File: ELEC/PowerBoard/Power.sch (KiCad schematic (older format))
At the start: 2 parts, among them J1 CONN_01X08, J2 CONN_01X08

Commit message: Added roadmap, worked on power board
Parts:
- added C1, C2, C3, C4: 220uF, Capacitors_SMD:CP_Elec_8x10.5, symbol CP
- added C5, C6, C7: 10uF, Capacitors_SMD:C_1206, symbol C
- added C8: 0.1uF, Capacitors_SMD:C_0805, symbol C
- added J3: Barrel_Jack, Connectors_Barrel.pretty:PJ-082BH, symbol Barrel_Jack
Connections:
- net +24V: now also C1.1, C2.1, C3.1, C4.1, C5.1, C6.1, C7.1, C8.1, J3.1
- net GND: now also C1.2, C2.2, C3.2, C4.2, C5.2, C6.2, C7.2, C8.2, J3.2, J3.3
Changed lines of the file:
@@
 LIBS:device
 LIBS:power
+LIBS:Power-cache
 EELAYER 25 0
 EELAYER END
@@
 NoConn ~ 2650 3650
 NoConn ~ 2650 3750
+$Comp
+L Barrel_Jack J3
+U 1 1 59628A55
+P 4500 3350
+F 0 "J3" H 4500 3560 50  0000 C CNN
+F 1 "Barrel_Jack" H 4500 3175 50  0000 C CNN
+F 2 "Connectors_Barrel.pretty:PJ-082BH" H 4550 3310 50  0001 C CNN
+F 3 "" H 4550 3310 50  0001 C CNN
+	1    4500 3350
+	1    0    0    -1
+$EndComp
+$Comp
+L +24V #PWR04
+U 1 1 59628BF8
+P 5200 3100
+F 0 "#PWR04" H 5200 2950 50  0001 C CNN
+F 1 "+24V" H 5200 3240 50  0000 C CNN
+F 2 "" H 5200 3100 50  0001 C CNN
+F 3 "" H 5200 3100 50  0001 C CNN
+	1    5200 3100
+	1    0    0    -1
+$EndComp
+Wire Wire Line
+	5200 3250 5200 3100
+Wire Wire Line
+	4800 3350 4800 3600
+Wire Wire Line
+	4800 3600 5200 3600
+Wire Wire Line
+	5200 3550 5200 3700
+Connection ~ 4800 3450
+$Comp
+L GND #PWR05
+U 1 1 59628CB8
+P 5200 3700
+F 0 "#PWR05" H 5200 3450 50  0001 C CNN
+F 1 "GND" H 5200 3550 50  0000 C CNN
+F 2 "" H 5200 3700 50  0001 C CNN
+F 3 "" H 5200 3700 50  0001 C CNN
+	1    5200 3700
+	1    0    0    -1
+$EndComp
+$Comp
+L CP C1
+U 1 1 59628D75
+P 5400 3400
+F 0 "C1" H 5425 3500 50  0000 L CNN
+F 1 "220uF" H 5425 3300 50  0000 L CNN
+F 2 "Capacitors_SMD:CP_Elec_8x10.5" H 5438 3250 50  0001 C CNN
+F 3 "" H 5400 3400 50  0001 C CNN
+F 4 "EEE-1VA221UP" H 5400 3400 60  0001 C CNN "Part Number"
+	1    5400 3400
+	1    0    0    -1
+$EndComp
+Connection ~ 5200 3250
+Connection ~ 5200 3600
+$Comp
+L C C6
+U 1 1 59628F1D
+P 6800 3400
+F 0 "C6" H 6825 3500 50  0000 L CNN
+F 1 "10uF" H 6825 3300 50  0000 L CNN
+F 2 "Capacitors_SMD:C_1206" H 6838 3250 50  0001 C CNN
+F 3 "" H 6800 3400 50  0001 C CNN
+	1    6800 3400
+	1    0    0    -1
+$EndComp
+$Comp
+L CP C2
+U 1 1 59629990
+P 5750 3400
+F 0 "C2" H 5775 3500 50  0000 L CNN
+F 1 "220uF" H 5775 3300 50  0000 L CNN
+F 2 "Capacitors_SMD:CP_Elec_8x10.5" H 5788 3250 50  0001 C CNN
+F 3 "" H 5750 3400 50  0001 C CNN
+F 4 "EEE-1VA221UP" H 5750 3400 60  0001 C CNN "Part Number"
+	1    5750 3400
+	1    0    0    -1
+$EndComp
+$Comp
+L CP C3
+U 1 1 596299C2
+P 6100 3400
+F 0 "C3" H 6125 3500 50  0000 L CNN
+F 1 "220uF" H 6125 3300 50  0000 L CNN
+F 2 "Capacitors_SMD:CP_Elec_8x10.5" H 6138 3250 50  0001 C CNN
+F 3 "" H 6100 3400 50  0001 C CNN
+F 4 "EEE-1VA221UP" H 6100 3400 60  0001 C CNN "Part Number"
+	1    6100 3400
+	1    0    0    -1
+$EndComp
+$Comp
+L CP C4
+U 1 1 596299F7
+P 6450 3400
+F 0 "C4" H 6475 3500 50  0000 L CNN
+F 1 "220uF" H 6475 3300 50  0000 L CNN
+F 2 "Capacitors_SMD:CP_Elec_8x10.5" H 6488 3250 50  0001 C CNN
+F 3 "" H 6450 3400 50  0001 C CNN
+F 4 "EEE-1VA221UP" H 6450 3400 60  0001 C CNN "Part Number"
+	1    6450 3400
+	1    0    0    -1
+$EndComp
+$Comp
+L C C5
+U 1 1 59629A98
+P 7100 3400
+F 0 "C5" H 7125 3500 50  0000 L CNN
+F 1 "10uF" H 7125 3300 50  0000 L CNN
+F 2 "Capacitors_SMD:C_1206" H 7138 3250 50  0001 C CNN
+F 3 "" H 7100 3400 50  0001 C CNN
+	1    7100 3400
+	1    0    0    -1
+$EndComp
+$Comp
+L C C7
+U 1 1 59629ADF
+P 7400 3400
+F 0 "C7" H 7425 3500 50  0000 L CNN
+F 1 "10uF" H 7425 3300 50  0000 L CNN
+F 2 "Capacitors_SMD:C_1206" H 7438 3250 50  0001 C CNN
+F 3 "" H 7400 3400 50  0001 C CNN
+	1    7400 3400
+	1    0    0    -1
+$EndComp
+$Comp
+L C C8
+U 1 1 59629B15
+P 7700 3400
+F 0 "C8" H 7725 3500 50  0000 L CNN
+F 1 "0.1uF" H 7725 3300 50  0000 L CNN
+F 2 "Capacitors_SMD:C_0805" H 7738 3250 50  0001 C CNN
+F 3 "" H 7700 3400 50  0001 C CNN
+	1    7700 3400
+	1    0    0    -1
+$EndComp
+Wire Wire Line
+	4800 3250 7700 3250
+Connection ~ 5400 3250
+Connection ~ 5750 3250
+Connection ~ 6100 3250
+Connection ~ 6450 3250
+Connection ~ 6800 3250
+Connection ~ 7100 3250
+Connection ~ 7400 3250
+Wire Wire Line
+	5200 3550 7700 3550
+Connection ~ 5400 3550
+Connection ~ 5750 3550
+Connection ~ 6100 3550
+Connection ~ 6450 3550
+Connection ~ 6800 3550
+Connection ~ 7100 3550
+Connection ~ 7400 3550
 $EndSCHEMATC

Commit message: Worked on power distrobution PCB
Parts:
- removed C5, C6, C7: 10uF, Capacitors_SMD:C_1206, symbol C
- removed C8: 0.1uF, Capacitors_SMD:C_0805, symbol C
- added J4: XT60 Connector, Connectors_Battery:XT60_Inline, symbol CONN_01X02
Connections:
- wire segments 20 -> 23
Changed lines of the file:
@@
 	1    0    0    -1
 $EndComp
-Wire Wire Line
-	2350 3050 2650 3050
 Text Label 2650 3050 0    60   ~ 0
 SYNC
@@
 	1    0    0    -1
 $EndComp
-Wire Wire Line
-	10250 3100 10250 3400
-Connection ~ 10250 3300
-Connection ~ 10250 3200
-Connection ~ 10250 3250
-Wire Wire Line
-	10250 3250 10050 3250
-Wire Wire Line
-	10050 3250 10050 3050
-Wire Wire Line
-	10250 3500 10250 3800
-Connection ~ 10250 3600
-Connection ~ 10250 3700
 $Comp
 L GND #PWR03
@@
 	1    0    0    -1
 $EndComp
-Wire Wire Line
-	10250 3650 10050 3650
-Wire Wire Line
-	10050 3650 10050 3850
-Connection ~ 10250 3650
 Text Label 2650 3250 0    60   ~ 0
 AUX_R
 Text Label 2650 3350 0    60   ~ 0
 AUX_L
-Wire Wire Line
-	2650 3250 2350 3250
-Wire Wire Line
-	2350 3350 2650 3350
-Wire Wire Line
-	2950 3150 2350 3150
-Wire Wire Line
-	2350 3450 2650 3450
-Wire Wire Line
-	2350 3550 2650 3550
-Wire Wire Line
-	2350 3650 2650 3650
-Wire Wire Line
-	2350 3750 2650 3750
 NoConn ~ 2650 3450
 NoConn ~ 2650 3550
@@
 	1    0    0    -1
 $EndComp
-Wire Wire Line
-	5200 3250 5200 3100
-Wire Wire Line
-	4800 3350 4800 3600
-Wire Wire Line
-	4800 3600 5200 3600
-Wire Wire Line
-	5200 3550 5200 3700
-Connection ~ 4800 3450
 $Comp
 L GND #PWR05
@@
 	1    0    0    -1
 $EndComp
-Connection ~ 5200 3250
-Connection ~ 5200 3600
-$Comp
-L C C6
-U 1 1 59628F1D
-P 6800 3400
-F 0 "C6" H 6825 3500 50  0000 L CNN
-F 1 "10uF" H 6825 3300 50  0000 L CNN
-F 2 "Capacitors_SMD:C_1206" H 6838 3250 50  0001 C CNN
-F 3 "" H 6800 3400 50  0001 C CNN
-	1    6800 3400
-	1    0    0    -1
-$EndComp
 $Comp
 L CP C2
@@
 $EndComp
 $Comp
-L C C5
-U 1 1 59629A98
-P 7100 3400
-F 0 "C5" H 7125 3500 50  0000 L CNN
-F 1 "10uF" H 7125 3300 50  0000 L CNN
-F 2 "Capacitors_SMD:C_1206" H 7138 3250 50  0001 C CNN
-F 3 "" H 7100 3400 50  0001 C CNN
-	1    7100 3400
-	1    0    0    -1
-$EndComp
-$Comp
-L C C7
-U 1 1 59629ADF
-P 7400 3400
-F 0 "C7" H 7425 3500 50  0000 L CNN
-F 1 "10uF" H 7425 3300 50  0000 L CNN
-F 2 "Capacitors_SMD:C_1206" H 7438 3250 50  0001 C CNN
-F 3 "" H 7400 3400 50  0001 C CNN
-	1    7400 3400
-	1    0    0    -1
-$EndComp
-$Comp
-L C C8
-U 1 1 59629B15
-P 7700 3400
-F 0 "C8" H 7725 3500 50  0000 L CNN
-F 1 "0.1uF" H 7725 3300 50  0000 L CNN
-F 2 "Capacitors_SMD:C_0805" H 7738 3250 50  0001 C CNN
-F 3 "" H 7700 3400 50  0001 C CNN
-	1    7700 3400
-	1    0    0    -1
-$EndComp
-Wire Wire Line
-	4800 3250 7700 3250
+L CONN_01X02 J4
+U 1 1 597010A4
+P 4500 4150
+F 0 "J4" H 4500 4300 50  0000 C CNN
+F 1 "XT60 Connector" H 4500 4400 50  0000 C CNN
+F 2 "Connectors_Battery:XT60_Inline" H 4500 4150 50  0001 C CNN
+F 3 "" H 4500 4150 50  0001 C CNN
+	1    4500 4150
+	-1   0    0    -1
+$EndComp
+$Comp
+L GND #PWR?
+U 1 1 59701954
+P 4850 4400
+F 0 "#PWR?" H 4850 4150 50  0001 C CNN
+F 1 "GND" H 4850 4250 50  0000 C CNN
+F 2 "" H 4850 4400 50  0001 C CNN
+F 3 "" H 4850 4400 50  0001 C CNN
+	1    4850 4400
+	1    0    0    -1
+$EndComp
+Wire Wire Line
+	2350 3050 2650 3050
+Wire Wire Line
+	10250 3100 10250 3400
+Connection ~ 10250 3300
+Connection ~ 10250 3200
+Connection ~ 10250 3250
+Wire Wire Line
+	10250 3250 10050 3250
+Wire Wire Line
+	10050 3250 10050 3050
+Wire Wire Line
+	10250 3500 10250 3800
+Connection ~ 10250 3600
+Connection ~ 10250 3700
+Wire Wire Line
+	10250 3650 10050 3650
+Wire Wire Line
+	10050 3650 10050 3850
+Connection ~ 10250 3650
+Wire Wire Line
+	2650 3250 2350 3250
+Wire Wire Line
+	2350 3350 2650 3350
+Wire Wire Line
+	2950 3150 2350 3150
+Wire Wire Line
+	2350 3450 2650 3450
+Wire Wire Line
+	2350 3550 2650 3550
+Wire Wire Line
+	2350 3650 2650 3650
+Wire Wire Line
+	2350 3750 2650 3750
+Wire Wire Line
+	5200 3250 5200 3100
+Wire Wire Line
+	4800 3350 4800 3600
+Wire Wire Line
+	4800 3600 5200 3600
+Wire Wire Line
+	5200 3550 5200 3700
+Connection ~ 4800 3450
+Connection ~ 5200 3250
+Connection ~ 5200 3600
+Wire Wire Line
+	4800 3250 6450 3250
 Connection ~ 5400 3250
 Connection ~ 5750 3250
 Connection ~ 6100 3250
-Connection ~ 6450 3250
-Connection ~ 6800 3250
-Connection ~ 7100 3250
-Connection ~ 7400 3250
-Wire Wire Line
-	5200 3550 7700 3550
 Connection ~ 5400 3550
 Connection ~ 5750 3550
 Connection ~ 6100 3550
-Connection ~ 6450 3550
-Connection ~ 6800 3550
-Connection ~ 7100 3550
-Connection ~ 7400 3550
+Wire Wire Line
+	5200 3550 6450 3550
+Wire Wire Line
+	4700 4200 4850 4200
+Wire Wire Line
+	4850 4200 4850 4400
+Wire Wire Line
+	4700 4100 5850 4100
 $EndSCHEMATC

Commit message: Did a whole whack on the power PCB
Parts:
- added J5: CONN_02X03, Pin_Headers:Pin_Header_Straight_2x03_Pitch1.27mm, symbol CONN_02X03
- added Q1: MOSFET_8PIN, Housings_SOIC.pretty:SOIC-8_3.9x4.9mm_Pitch1.27mm, symbol MOSFET_8PIN
- added R1, R5, R6, R7, Ry1: 1M, Resistors_SMD:R_0805, symbol R
- added R2: 422K, Resistors_SMD:R_0805, symbol R
- added R3: 316K, Resistors_SMD:R_0805, symbol R
- added R4: 243K, Resistors_SMD:R_0805, symbol R
- added Rh1: 1.32M, Resistors_SMD:R_0805, symbol R
- added Rx1: 220K, Resistors_SMD:R_0805, symbol R
- added U1: LM9036MX, Housings_SOIC.pretty:SOIC-8_3.9x4.9mm_Pitch1.27mm, symbol LM9036MX
- added U2: LMV358, Housings_SOIC.pretty:SOIC-8_3.9x4.9mm_Pitch1.27mm, symbol LMV358
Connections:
- net labels added: +5V, Vref
- wire segments 23 -> 85
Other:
- note added: "4,5,6 cell selector"
- note added: "WARNING: Never plug in XT60 connector (Battery) at time same time as the barrel jack!!!"
- moved on the sheet: C1, C2, C3, C4, J3, J4

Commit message: Finished Power PCB
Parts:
- added C10: 1uF, Capacitors_SMD:C_0805, symbol C
- added C5, C7, C9: 100nF, Capacitors_SMD:C_0805, symbol C
- added C6, C8: 10uF, Capacitors_SMD:C_0805, symbol C
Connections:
- net +24V: now also C5.1, C6.1
- net +5V: now also C10.1, C7.1, C8.1, C9.1
- net GND: now also C10.2, C5.2, C6.2, C7.2, C8.2, C9.2
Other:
- moved on the sheet: J5, R1, R2, R3, R4

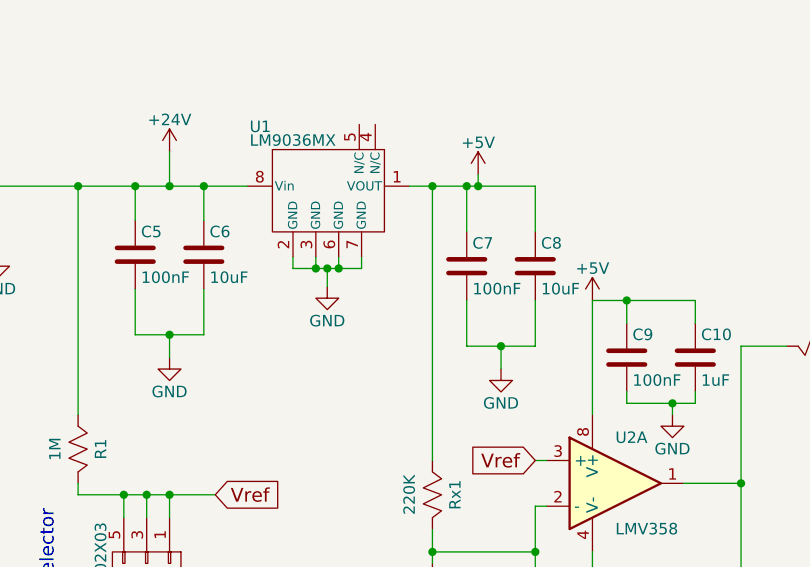
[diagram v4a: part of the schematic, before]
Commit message: -Filled in P/N -Generated BOM -Ordered PCBs
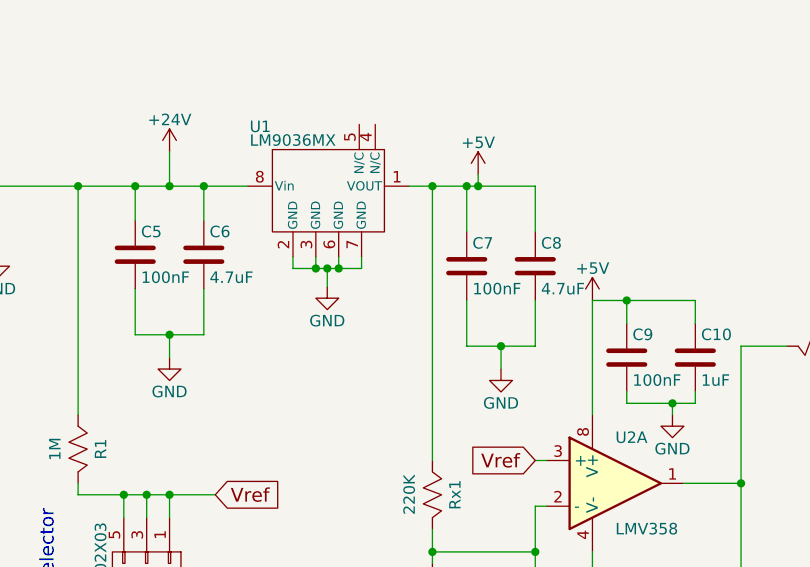
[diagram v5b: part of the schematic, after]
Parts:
- C10: Part Number (none) -> CL21B105KBFNNNE
- C5, C7, C9: Part Number (none) -> CL21B103KBANNNC
- C6, C8: value 10uF -> 4.7uF; Part Number (none) -> CL21A475KLCLQNC
- J3: Part Number (none) -> PJ-082BH
- J5: Part Number (none) -> 20021111-00006T4LF
- Q1: Part Number (none) -> AO4576
- R1, R5, R6, R7, Ry1: Part Number (none) -> ERJ-6GEYJ105V
- R2: Part Number (none) -> ERJ-6ENF4223V
- R3: Part Number (none) -> ERJ-6ENF3163V
- R4: Part Number (none) -> ERJ-6ENF2433V
- Rh1: Part Number (none) -> ERJ-6ENF1334V
- Rx1: Part Number (none) -> ERJ-6GEYJ224V
- U1: Part Number (none) -> LM9036MX-5.0/NOPB
- U2: Part Number (none) -> LMV358MX/NOPB
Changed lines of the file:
@@
 SYNC
 $Comp
-L GNDA #PWR1
+L GNDA #PWR01
 U 1 1 593E4897
 P 2950 3150
-F 0 "#PWR1" H 2950 2900 50  0001 C CNN
+F 0 "#PWR01" H 2950 2900 50  0001 C CNN
 F 1 "GNDA" V 2950 2900 50  0000 C CNN
 F 2 "" H 2950 3150 50  0001 C CNN
@@
 $EndComp
 $Comp
-L +24V #PWR19
+L +24V #PWR02
 U 1 1 593E5732
 P 10050 3050
-F 0 "#PWR19" H 10050 2900 50  0001 C CNN
+F 0 "#PWR02" H 10050 2900 50  0001 C CNN
 F 1 "+24V" H 10050 3190 50  0000 C CNN
 F 2 "" H 10050 3050 50  0001 C CNN
@@
 F 2 "Connectors_Barrel.pretty:PJ-082BH" H 4600 2410 50  0001 C CNN
 F 3 "" H 4600 2410 50  0001 C CNN
+F 4 "PJ-082BH" H 4550 2450 60  0001 C CNN "Part Number"
 	1    4550 2450
 	1    0    0    -1
 $EndComp
 $Comp
-L +24V #PWR7
+L +24V #PWR03
 U 1 1 59628BF8
 P 5250 2200
-F 0 "#PWR7" H 5250 2050 50  0001 C CNN
+F 0 "#PWR03" H 5250 2050 50  0001 C CNN
 F 1 "+24V" H 5250 2340 50  0000 C CNN
 F 2 "" H 5250 2200 50  0001 C CNN
@@
 $EndComp
 $Comp
-L GND #PWR8
+L GND #PWR04
 U 1 1 59628CB8
 P 5250 2800
-F 0 "#PWR8" H 5250 2550 50  0001 C CNN
+F 0 "#PWR04" H 5250 2550 50  0001 C CNN
 F 1 "GND" H 5250 2650 50  0000 C CNN
 F 2 "" H 5250 2800 50  0001 C CNN
@@
 $EndComp
 $Comp
-L GND #PWR2
+L GND #PWR05
 U 1 1 59701954
 P 3400 4550
-F 0 "#PWR2" H 3400 4300 50  0001 C CNN
+F 0 "#PWR05" H 3400 4300 50  0001 C CNN
 F 1 "GND" H 3400 4400 50  0000 C CNN
 F 2 "" H 3400 4550 50  0001 C CNN
@@
 $EndComp
 $Comp
-L GND #PWR6
+L GND #PWR06
 U 1 1 598A7FE8
 P 4840 4690
-F 0 "#PWR6" H 4840 4440 50  0001 C CNN
+F 0 "#PWR06" H 4840 4440 50  0001 C CNN
 F 1 "GND" H 4840 4540 50  0000 C CNN
 F 2 "" H 4840 4690 50  0001 C CNN
@@
 $EndComp
 $Comp
-L +5V #PWR10
+L +5V #PWR07
 U 1 1 598A84C1
 P 5500 4200
-F 0 "#PWR10" H 5500 4050 50  0001 C CNN
+F 0 "#PWR07" H 5500 4050 50  0001 C CNN
 F 1 "+5V" H 5500 4340 50  0000 C CNN
 F 2 "" H 5500 4200 50  0001 C CNN
@@
 F 2 "Housings_SOIC.pretty:SOIC-8_3.9x4.9mm_Pitch1.27mm" H 6100 5550 50  0001 C CNN
 F 3 "" H 6100 5550 50  0001 C CNN
+F 4 "LMV358MX/NOPB" H 6100 5550 60  0001 C CNN "Part Number"
 	1    6100 5550
 	1    0    0    -1
@@
 F 2 "Resistors_SMD:R_0805" V 3680 5400 50  0001 C CNN
 F 3 "" H 3750 5400 50  0001 C CNN
+F 4 "ERJ-6GEYJ105V" V 3750 5400 60  0001 C CNN "Part Number"
 	1    3750 5400
 	1    0    0    -1
@@
 F 2 "Resistors_SMD:R_0805" V 3680 6600 50  0001 C CNN
 F 3 "" H 3750 6600 50  0001 C CNN
+F 4 "ERJ-6ENF4223V" V 3750 6600 60  0001 C CNN "Part Number"
 	1    3750 6600
 	1    0    0    -1
 $EndComp
 $Comp
-L +5V #PWR12
+L +5V #PWR08
 U 1 1 598A865B
 P 6000 4750
-F 0 "#PWR12" H 6000 4600 50  0001 C CNN
+F 0 "#PWR08" H 6000 4600 50  0001 C CNN
 F 1 "+5V" H 6000 4890 50  0000 C CNN
 F 2 "" H 6000 4750 50  0001 C CNN
@@
 $EndComp
 $Comp
-L GND #PWR13
+L GND #PWR09
 U 1 1 598A86D5
 P 6000 6000
-F 0 "#PWR13" H 6000 5750 50  0001 C CNN
+F 0 "#PWR09" H 6000 5750 50  0001 C CNN
 F 1 "GND" H 6000 5850 50  0000 C CNN
 F 2 "" H 6000 6000 50  0001 C CNN
@@
 F 2 "Resistors_SMD:R_0805" V 3980 6600 50  0001 C CNN
 F 3 "" H 4050 6600 50  0001 C CNN
+F 4 "ERJ-6ENF3163V" V 4050 6600 60  0001 C CNN "Part Number"
 	1    4050 6600
 	1    0    0    -1
@@
 F 2 "Resistors_SMD:R_0805" V 4280 6600 50  0001 C CNN
 F 3 "" H 4350 6600 50  0001 C CNN
+F 4 "ERJ-6ENF2433V" V 4350 6600 60  0001 C CNN "Part Number"
 	1    4350 6600
 	1    0    0    -1
@@
 F 2 "Pin_Headers:Pin_Header_Straight_2x03_Pitch1.27mm" H 4050 4750 50  0001 C CNN
 F 3 "" H 4050 4750 50  0001 C CNN
+F 4 "20021111-00006T4LF" H 4050 5950 60  0001 C CNN "Part Number"
 	1    4050 5950
 	0    1    1    0
 $EndComp
 $Comp
-L GND #PWR3
+L GND #PWR010
 U 1 1 598A9A51
 P 4050 6900
-F 0 "#PWR3" H 4050 6650 50  0001 C CNN
+F 0 "#PWR010" H 4050 6650 50  0001 C CNN
 F 1 "GND" H 4050 6750 50  0000 C CNN
 F 2 "" H 4050 6900 50  0001 C CNN
@@
 F 2 "Resistors_SMD:R_0805" V 5230 5600 50  0001 C CNN
 F 3 "" H 5300 5600 50  0001 C CNN
+F 4 "ERJ-6GEYJ224V" V 5300 5600 60  0001 C CNN "Part Number"
 	1    5300 5600
 	1    0    0    -1
@@
 F 2 "Resistors_SMD:R_0805" V 5230 6050 50  0001 C CNN
 F 3 "" H 5300 6050 50  0001 C CNN
+F 4 "ERJ-6GEYJ105V" V 5300 6050 60  0001 C CNN "Part Number"
 	1    5300 6050
 	1    0    0    -1
@@
 F 2 "Resistors_SMD:R_0805" V 6130 6400 50  0001 C CNN
 F 3 "" H 6200 6400 50  0001 C CNN
+F 4 "ERJ-6ENF1334V" V 6200 6400 60  0001 C CNN "Part Number"
 	1    6200 6400
 	0    1    1    0
 $EndComp
 $Comp
-L GND #PWR9
+L GND #PWR011
 U 1 1 598AB730
 P 5300 6300
-F 0 "#PWR9" H 5300 6050 50  0001 C CNN
+F 0 "#PWR011" H 5300 6050 50  0001 C CNN
 F 1 "GND" H 5300 6150 50  0000 C CNN
 F 2 "" H 5300 6300 50  0001 C CNN
@@
 $EndComp
 $Comp
-L GND #PWR15
+L GND #PWR012
 U 1 1 598AC230
 P 7300 5900
-F 0 "#PWR15" H 7300 5650 50  0001 C CNN
+F 0 "#PWR012" H 7300 5650 50  0001 C CNN
 F 1 "GND" H 7300 5750 50  0000 C CNN
 F 2 "" H 7300 5900 50  0001 C CNN
@@
 $EndComp
 $Comp
-L GND #PWR16
+L GND #PWR013
 U 1 1 598AC274
 P 7800 5100
-F 0 "#PWR16" H 7800 4850 50  0001 C CNN
+F 0 "#PWR013" H 7800 4850 50  0001 C CNN
 F 1 "GND" H 7800 4950 50  0000 C CNN
 F 2 "" H 7800 5100 50  0001 C CNN
@@
 $EndComp
 $Comp
-L +5V #PWR17
+L +5V #PWR014
 U 1 1 598AC328
 P 7800 6050
-F 0 "#PWR17" H 7800 5900 50  0001 C CNN
+F 0 "#PWR014" H 7800 5900 50  0001 C CNN
 F 1 "+5V" H 7800 6190 50  0000 C CNN
 F 2 "" H 7800 6050 50  0001 C CNN
@@
 F 2 "Resistors_SMD:R_0805" V 6930 4950 50  0001 C CNN
 F 3 "" H 7000 4950 50  0001 C CNN
+F 4 "ERJ-6GEYJ105V" V 7000 4950 60  0001 C CNN "Part Number"
 	1    7000 4950
 	0    1    1    0
@@
 F 2 "Resistors_SMD:R_0805" V 7930 4950 50  0001 C CNN
 F 3 "" H 8000 4950 50  0001 C CNN
+F 4 "ERJ-6GEYJ105V" V 8000 4950 60  0001 C CNN "Part Number"
 	1    8000 4950
 	0    1    1    0
@@
 F 2 "Housings_SOIC.pretty:SOIC-8_3.9x4.9mm_Pitch1.27mm" H 4878 4100 50  0001 C CNN
 F 3 "" H 4840 4250 50  0001 C CNN
+F 4 "LM9036MX-5.0/NOPB" H 4840 4250 60  0001 C CNN "Part Number"
 	1    4840 4250
 	1    0    0    -1
@@
 F 2 "Resistors_SMD:R_0805" V 8580 5550 50  0001 C CNN
 F 3 "" H 8650 5550 50  0001 C CNN
+F 4 "ERJ-6GEYJ105V" V 8650 5550 60  0001 C CNN "Part Number"
 	1    8650 5550
 	-1   0    0    1
 $EndComp
 $Comp
-L GND #PWR18
+L GND #PWR015
 U 1 1 598B1935
 P 8880 5850
-F 0 "#PWR18" H 8880 5600 50  0001 C CNN
+F 0 "#PWR015" H 8880 5600 50  0001 C CNN
 F 1 "GND" H 8880 5700 50  0000 C CNN
 F 2 "" H 8880 5850 50  0001 C CNN
@@
 $EndComp
 $Comp
-L +24V #PWR4
+L +24V #PWR016
 U 1 1 598B2833
 P 4150 4100
-F 0 "#PWR4" H 4150 3950 50  0001 C CNN
+F 0 "#PWR016" H 4150 3950 50  0001 C CNN
 F 1 "+24V" H 4150 4240 50  0000 C CNN
 F 2 "" H 4150 4100 50  0001 C CNN
@@
 F 2 "Housings_SOIC.pretty:SOIC-8_3.9x4.9mm_Pitch1.27mm" H 9010 5330 50  0001 C CNN
 F 3 "" H 9000 5250 50  0001 C CNN
+F 4 "AO4576" H 9000 5250 60  0001 C CNN "Part Number"
 	1    9000 5250
 	1    0    0    -1
@@
 F 2 "Capacitors_SMD:C_0805" H 4038 4400 50  0001 C CNN
 F 3 "" H 4000 4550 50  0001 C CNN
+F 4 "CL21B103KBANNNC" H 4000 4550 60  0001 C CNN "Part Number"
 	1    4000 4550
 	1    0    0    -1
@@
 P 4300 4550
 F 0 "C6" H 4325 4650 50  0000 L CNN
-F 1 "10uF" H 4325 4450 50  0000 L CNN
+F 1 "4.7uF" H 4325 4450 50  0000 L CNN
 F 2 "Capacitors_SMD:C_0805" H 4338 4400 50  0001 C CNN
 F 3 "" H 4300 4550 50  0001 C CNN
+F 4 "CL21A475KLCLQNC" H 4300 4550 60  0001 C CNN "Part Number"
 	1    4300 4550
 	1    0    0    -1
@@
 	4000 4900 4300 4900
 $Comp
-L GND #PWR5
+L GND #PWR017
 U 1 1 598D23CC
 P 4150 5000
-F 0 "#PWR5" H 4150 4750 50  0001 C CNN
+F 0 "#PWR017" H 4150 4750 50  0001 C CNN
 F 1 "GND" H 4150 4850 50  0000 C CNN
 F 2 "" H 4150 5000 50  0001 C CNN
@@
 F 2 "Capacitors_SMD:C_0805" H 5488 4450 50  0001 C CNN
 F 3 "" H 5450 4600 50  0001 C CNN
+F 4 "CL21B103KBANNNC" H 5450 4600 60  0001 C CNN "Part Number"
 	1    5450 4600
 	1    0    0    -1
@@
 P 5750 4600
 F 0 "C8" H 5775 4700 50  0000 L CNN
-F 1 "10uF" H 5775 4500 50  0000 L CNN
+F 1 "4.7uF" H 5775 4500 50  0000 L CNN
 F 2 "Capacitors_SMD:C_0805" H 5788 4450 50  0001 C CNN
 F 3 "" H 5750 4600 50  0001 C CNN
+F 4 "CL21A475KLCLQNC" H 5750 4600 60  0001 C CNN "Part Number"
 	1    5750 4600
 	1    0    0    -1
@@
 	5450 4950 5750 4950
 $Comp
-L GND #PWR11
+L GND #PWR018
 U 1 1 598D2618
 P 5600 5050
-F 0 "#PWR11" H 5600 4800 50  0001 C CNN
+F 0 "#PWR018" H 5600 4800 50  0001 C CNN
 F 1 "GND" H 5600 4900 50  0000 C CNN
 F 2 "" H 5600 5050 50  0001 C CNN
@@
 F 2 "Capacitors_SMD:C_0805" H 6188 4850 50  0001 C CNN
 F 3 "" H 6150 5000 50  0001 C CNN
+F 4 "CL21B103KBANNNC" H 6150 5000 60  0001 C CNN "Part Number"
 	1    6150 5000
 	1    0    0    -1
@@
 F 2 "Capacitors_SMD:C_0805" H 6488 4850 50  0001 C CNN
 F 3 "" H 6450 5000 50  0001 C CNN
+F 4 "CL21B105KBFNNNE" H 6450 5000 60  0001 C CNN "Part Number"
 	1    6450 5000
 	1    0    0    -1
@@
 	6450 5200 6450 5150
 $Comp
-L GND #PWR14
+L GND #PWR019
 U 1 1 598D2C63
 P 6350 5250
-F 0 "#PWR14" H 6350 5000 50  0001 C CNN
+F 0 "#PWR019" H 6350 5000 50  0001 C CNN
 F 1 "GND" H 6350 5100 50  0000 C CNN
 F 2 "" H 6350 5250 50  0001 C CNN
